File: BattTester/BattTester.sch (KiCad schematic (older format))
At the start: 25 parts, among them J1 Battery, J2 SD_Card, J3 PWR, J4 UPDI, Q1 IRLZ44N, U1 LTC1286CN8, U2 ATtiny1624-SS, U3 LD1086DT33, U4 LM358AN

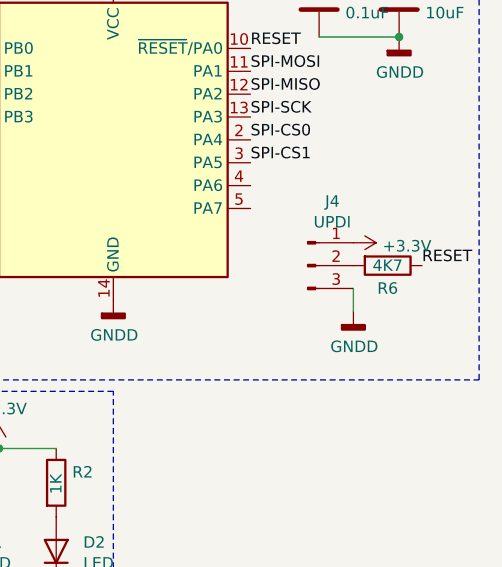
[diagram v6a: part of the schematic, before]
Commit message: fix updi header
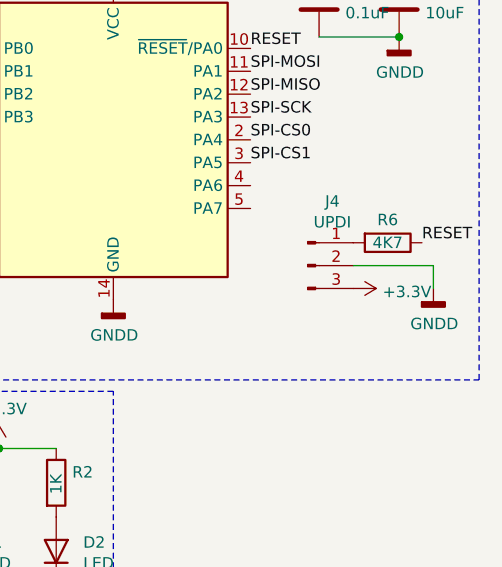
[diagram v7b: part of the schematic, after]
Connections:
- net +3V3: now also J4.3 (Pin_3); no longer J4.1 (Pin_1)
- net GND: now also J4.2 (Pin_2); no longer J4.3 (Pin_3)
- net at R6.2: now also J4.1 (Pin_1); no longer J4.2 (Pin_2)
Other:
- moved on the sheet: R6
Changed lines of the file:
@@
 L power:+3.3V #PWR0116
 U 1 1 6170BAF0
-P 7450 1950
-F 0 "#PWR0116" H 7450 1800 50  0001 C CNN
-F 1 "+3.3V" V 7465 2078 50  0000 L CNN
-F 2 "" H 7450 1950 50  0001 C CNN
-F 3 "" H 7450 1950 50  0001 C CNN
-	1    7450 1950
+P 7450 2150
+F 0 "#PWR0116" H 7450 2000 50  0001 C CNN
+F 1 "+3.3V" V 7465 2278 50  0000 L CNN
+F 2 "" H 7450 2150 50  0001 C CNN
+F 3 "" H 7450 2150 50  0001 C CNN
+	1    7450 2150
 	0    1    1    0
 $EndComp
@@
 L Device:R R6
 U 1 1 6170C3BE
-P 7600 2050
-F 0 "R6" V 7700 2050 50  0000 C CNN
-F 1 "4K7" V 7600 2050 50  0000 C CNN
-F 2 "Resistor_SMD:R_1206_3216Metric_Pad1.30x1.75mm_HandSolder" V 7530 2050 50  0001 C CNN
-F 3 "~" H 7600 2050 50  0001 C CNN
-	1    7600 2050
+P 7600 1950
+F 0 "R6" V 7500 1950 50  0000 C CNN
+F 1 "4K7" V 7600 1950 50  0000 C CNN
+F 2 "Resistor_SMD:R_1206_3216Metric_Pad1.30x1.75mm_HandSolder" V 7530 1950 50  0001 C CNN
+F 3 "~" H 7600 1950 50  0001 C CNN
+	1    7600 1950
 	0    1    1    0
 $EndComp
 Wire Wire Line
-	7450 2150 7450 2250
+	7800 2050 7800 2150
 $Comp
 L power:GNDD #PWR0117
 U 1 1 6170DFCD
-P 7450 2250
-F 0 "#PWR0117" H 7450 2000 50  0001 C CNN
-F 1 "GNDD" H 7454 2095 50  0000 C CNN
-F 2 "" H 7450 2250 50  0001 C CNN
-F 3 "" H 7450 2250 50  0001 C CNN
-	1    7450 2250
-	1    0    0    -1
-$EndComp
-Text Label 7750 2050 0    50   ~ 0
+P 7800 2150
+F 0 "#PWR0117" H 7800 1900 50  0001 C CNN
+F 1 "GNDD" H 7804 1995 50  0000 C CNN
+F 2 "" H 7800 2150 50  0001 C CNN
+F 3 "" H 7800 2150 50  0001 C CNN
+	1    7800 2150
+	1    0    0    -1
+$EndComp
+Text Label 7750 1950 0    50   ~ 0
 RESET
 $Comp
@@
 	1    0    0    -1
 $EndComp
+Wire Wire Line
+	7800 2050 7450 2050
 $EndSCHEMATC

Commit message: minor sch edit
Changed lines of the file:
@@
 	4550 900  3700 900
-Wire Wire Line
-	3400 1900 3400 1800
-Wire Wire Line
-	3400 1800 3250 1800
 Wire Wire Line
 	3700 1900 3700 1800
@@
 	1000 1150 1100 1150
 Wire Wire Line
-	3400 1900 3700 1900
-Wire Wire Line
 	3250 1700 3700 1700
 $Comp
@@
 Wire Wire Line
 	7800 2050 7450 2050
+Connection ~ 3700 1800
+Wire Wire Line
+	3250 1800 3700 1800
 $EndSCHEMATC
